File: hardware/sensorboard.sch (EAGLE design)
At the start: 22 parts, among them U3 QRE1113, U4 QRE1113, U5 QRE1113, U6 QRE1113, U7 QRE1113, U8 QRE1113, U9 QRE1113

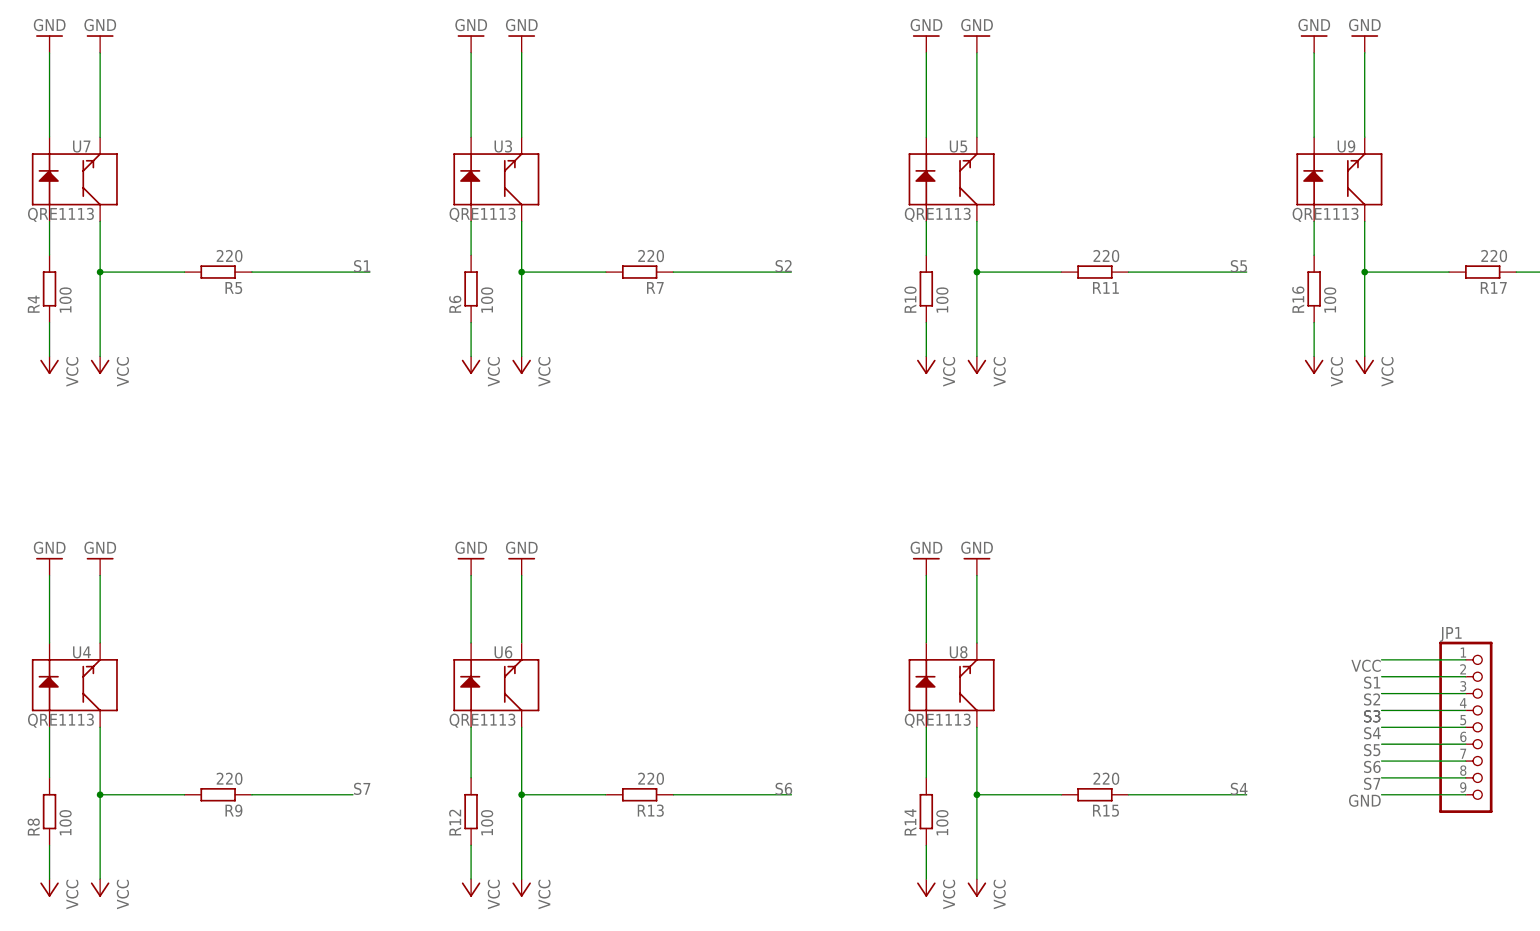
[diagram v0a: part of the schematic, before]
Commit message: Added capacitors to sensor board. Fixed routing.
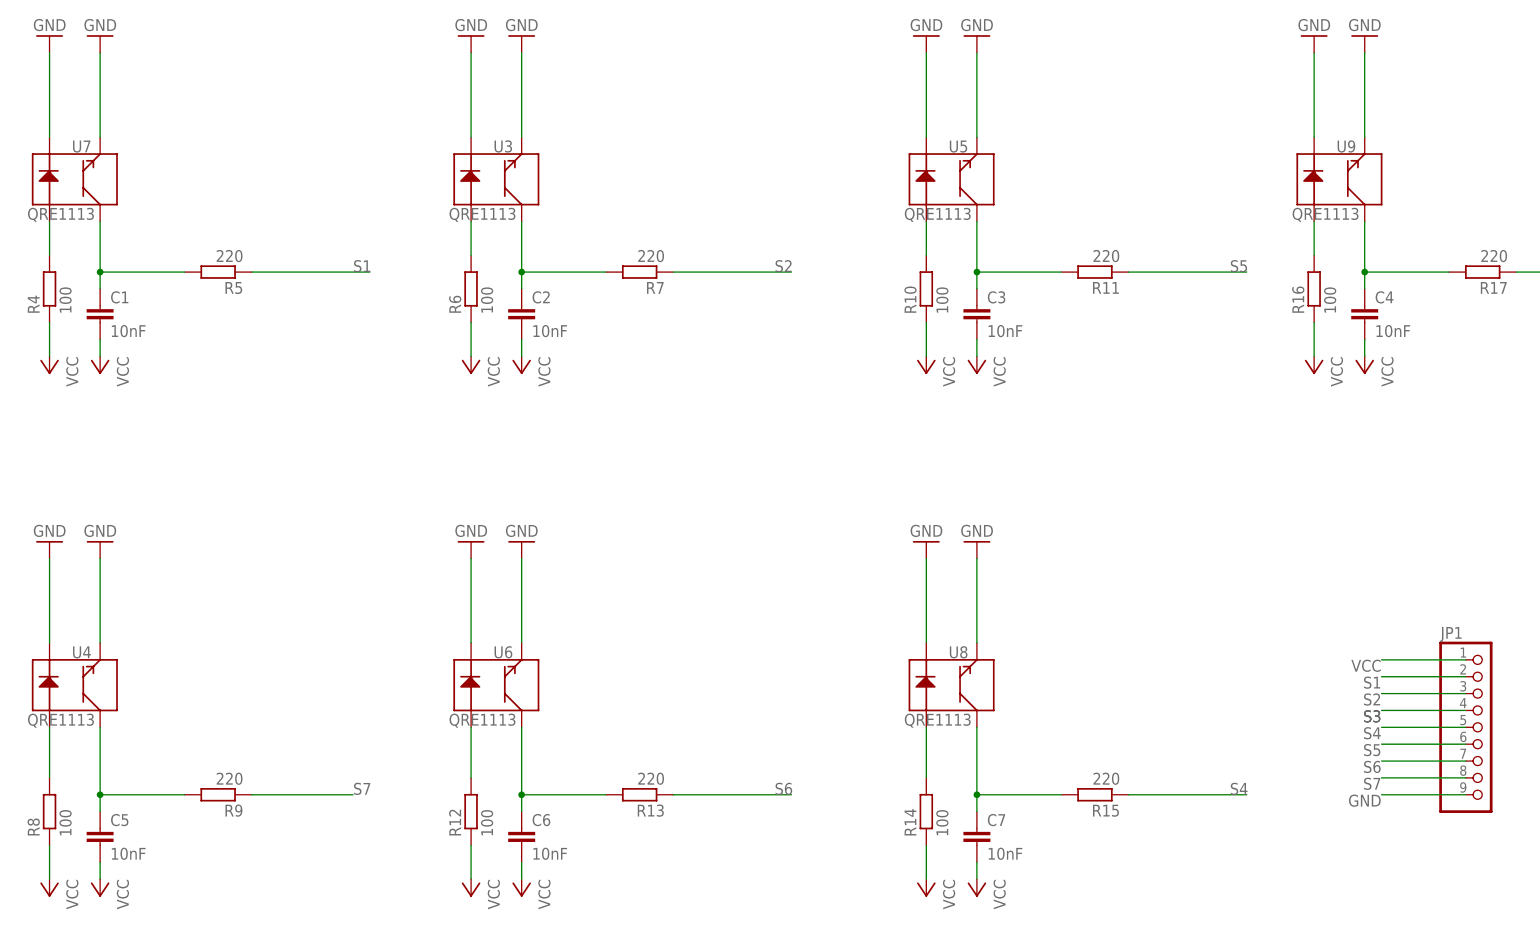
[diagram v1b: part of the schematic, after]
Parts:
- added C1, C2, C3, C4, C5, C6, C7: 10nF, resistor:C-EUC0805K
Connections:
- new net N$1: C1.1, R5.2, U7.C
- new net N$2: C2.1, R7.2, U3.C
- new net N$3: C3.1, R11.2, U5.C
- new net N$4: C4.1, R17.2, U9.C
- new net N$5: C7.1, R15.2, U8.C
- new net N$6: C6.1, R13.2, U6.C
- new net N$7: C5.1, R9.2, U4.C
- net VCC: now also C1.2, C2.2, C3.2, C4.2, C5.2, C6.2, C7.2; no longer R11.2, R13.2, R15.2, R17.2, R5.2, R7.2, R9.2, U3.C, U4.C, U5.C, U6.C, U7.C, U8.C, U9.C

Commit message: Beautified sensorboard and motherboard schematics. Fixed motherboard angle error.
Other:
- moved on the sheet: C1, C2, C3, C4, C5, C6, C7, JP1, R10, R11, R12, R13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
